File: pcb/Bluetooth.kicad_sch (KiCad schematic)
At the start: 20 parts, among them U5 RN4678

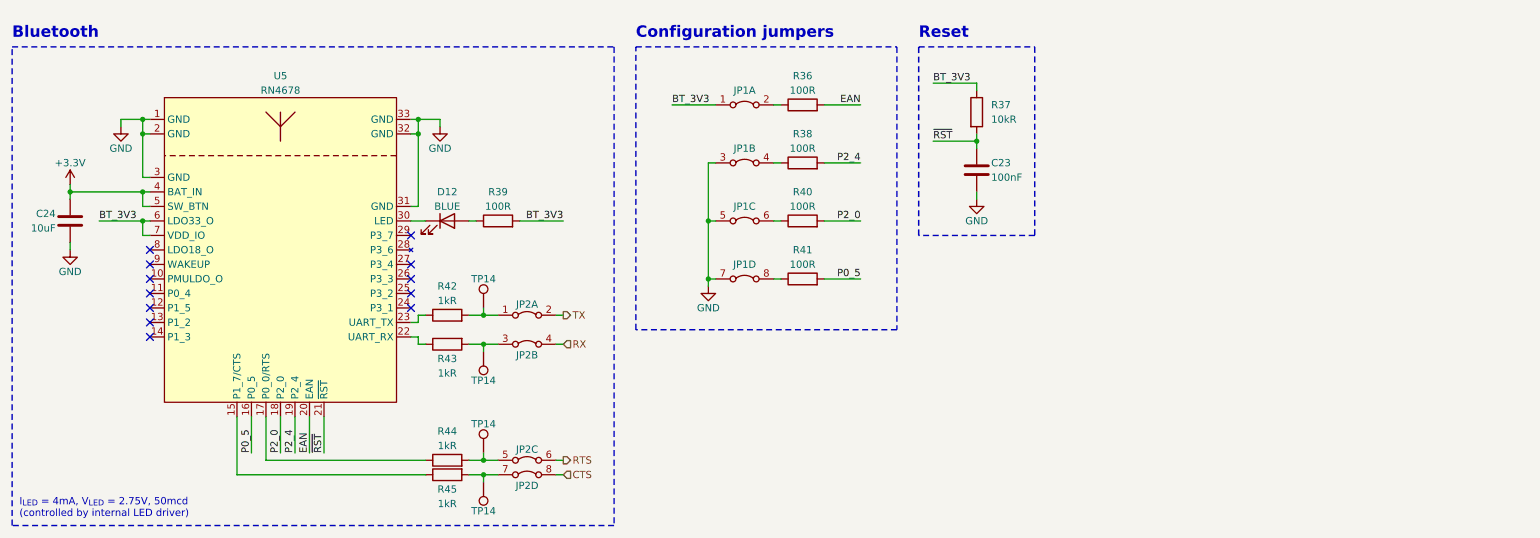
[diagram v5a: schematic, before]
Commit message: [pcb] Start reworking pcb with 0603 components
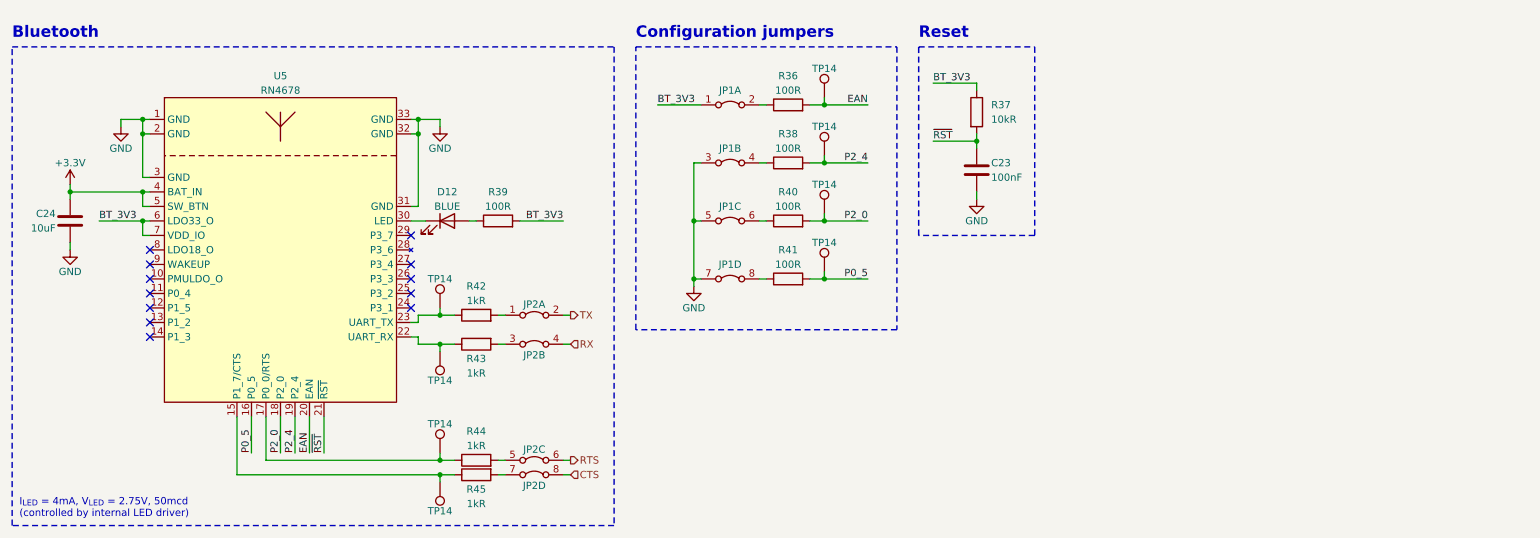
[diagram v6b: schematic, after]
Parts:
- added TP14 (x4): TestPoint, TestPoint:TestPoint_Pad_D1.5mm, symbol Connector:TestPoint
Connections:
- net EAN: now also TP14.1
- net P0_5: now also TP14.1
- net P2_0: now also TP14.1
- net P2_4: now also TP14.1
- net at JP2.3, R43.2: no longer TP14.1
- net at R45.1, U5.15 (P1_7/CTS): now also TP14.1
- net at R44.1, U5.17 (P0_0/RTS): now also TP14.1
- net at R43.1, U5.22 (UART_RX): now also TP14.1
- net at R42.1, U5.23 (UART_TX): now also TP14.1
- net at JP2.7, R45.2: no longer TP14.1
- net at JP2.1, R42.2: no longer TP14.1
- net at JP2.5, R44.2: no longer TP14.1
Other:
- moved on the sheet: JP1A, JP1B, JP1C, JP1D, JP2A, JP2B, JP2C, JP2D, R36, R38, R40, R41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
